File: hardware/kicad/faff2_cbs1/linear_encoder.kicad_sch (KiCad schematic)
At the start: 26 parts, among them J601 FH12-10S-0.5SH(55), J602 FTSH-105-01-L-DV-K-TR, U601 AM26LV32

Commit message: review r1: logic-analyser headers, U501 reference note, AFE/encoder fixes
Answers the captain's round-1 review points on loadcell_afe, linear_encoder,
temp_sense and nvm_calibration.

U501 and the reference (R1). The ADS1235 has no internal reference and no
reference output pin - REFP0/REFN0 are inputs. The reference is the load cell's
own excitation, sensed at the bridge, which is what makes the measurement
ratiometric. Documented in a 15-line note beside U501B's reference pins.

Logic-analyser headers (R2, R5). The Amodo keyed 10-way 0.1in socket
(8510-4500PL) replaces the per-net hooks:

  J502  loadcell_afe   CH0..CH7 = the whole SPI3 interface plus nDRDY, START,
                       nRESET and CLKIN; TP506..TP512 and TP514 removed
  J603  linear_encoder CH0..CH4 = the three receiver outputs plus ENC_SDO and
                       ENC_nPROG; TP602..TP607 removed

Both tap the driver side of the series terminators, so the header still sees the
bus when an isolation link is lifted. J602 is KEPT: it carries REQ-PS-09, its
pin 9 is +5V_ENC where the socket wants GND, and six of its signals are the
terminated RS-422 pairs that DEC-0018 ruling 1 keeps stub-free. Raised as a
decision; ruled option (a) and captain-ratified.

J601 (R3, R4). Reference text moved off the body; the project-local
FH12-10S-0.5SH(55) symbol now shows pin numbers and names every pin (1..10,
MP1/MP2), matching the FH35C house exemplar. Fixed in faff2_periph.kicad_sym
and in the sheet's embedded copy, so no lib_symbol_mismatch.

5 V read-head supply (R6). R608, R609 and D602 are DNP parallel positions on
R601, FB601 and D601. Not for current sharing - the ferrite alone has 4x margin
on the CALC budget - but for bring-up: a shunt at R608 meters head current in
circuit, R609 bypasses the bead, D602 is a second SC-79 clamp. Moving D601 up
to make room also cleared its value text off the ENC_nPROG label and its ground
triangle off the ENC_nPROG wire.

temp_sense C701/C702 (R7). Both had their groun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
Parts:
- removed TP602: TestPoint, Amodo:TestPoint_Pad_D1.0mm, symbol Amodo_Connectors:TestPoint
- removed TP603, TP604, TP605, TP606, TP607: TestPoint, Amodo:KeystoneMiniatureTestLoop, symbol Amodo_Connectors:TestPointHook
- added D602: PESD5V0U1UB, Amodo:SC-79 (SOD523), symbol Amodo_Diodes:PESD5V0U1UB
- added J603: 8510-4500PL, Amodo:8510-4500PL_LOGIC_TEST, symbol Amodo_Connectors:Header_Female_10-way_2-row_Straight_2.54mm_THT__KEYED_LOGIC_TE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
- added R608, R609: 0R, Amodo:R_0603_1608Metric, symbol Amodo_Resistors:RES_TF_0R_0603
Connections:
- net +5V: now also R608.1
- net +5V_ENC: now also D602.1 (K), R609.2
- net ENC_SDO: now also J603.4 (CH3)
- net ENC_nPROG: now also J603.5 (CH4)
- net GND: now also D602.2 (A), J603.10 (GND), J603.9 (GND)
- net LINEAR_ENCODER_A: now also J603.1 (CH0)
- net LINEAR_ENCODER_B: now also J603.2 (CH1)
- net LINEAR_ENCODER_Z: now also J603.3 (CH2)
- net at FB601.1, R601.2: now also R608.2, R609.1
- no-connect marks 1 -> 4
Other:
- note added: "J603 - LOGIC-ANALYSER HEADER Amodo keyed 0.1in socket, 8510-4500PL. One plug replaces the old TP602..TP607 hooks, so a logic analyser goes on in one go. CH0 LINEAR_ENCODER_A CH1 LINEAR_ENCODER_B CH2 LINEAR_ENCODER_Z CH3 ENC_SDO CH4 ENC_nPROG CH5..CH7 spare (no-connect) 9, 10 GND for the leads Only single-ended nets are tapped: a 2.54 mm stub on a terminated 1 MHz RS-422 pair is the discontinuity 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"
- note added: "R608 / R609 / D602 are DNP parallel positions on R601 / FB601 / D601. Fit a shunt at R608 and lift R601 to meter head current in circuit; fit R609 to bypass the bead; D602 is a second SC-79 clamp position. None fitted by default."
- note removed: "GND hooks for scope / logic-analyser clips."
- moved on the sheet: D601, TP601

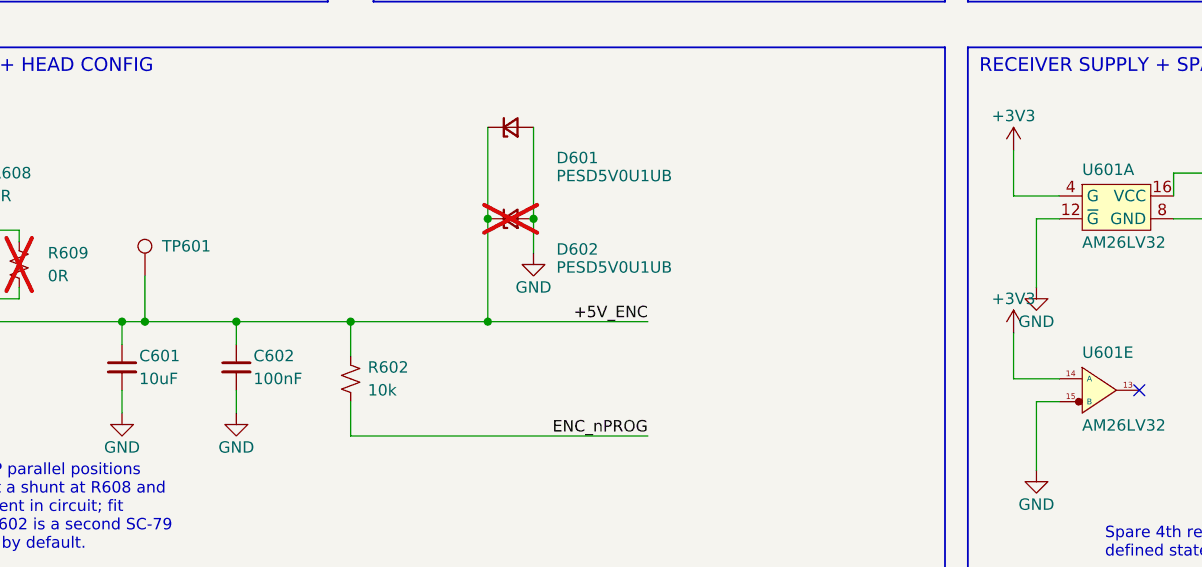
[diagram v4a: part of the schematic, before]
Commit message: review r1 final sweep: power labels, TP silkscreen names, text overlaps
The captain's design-wide pass, run once the per-sheet batches had landed.
Presentation only: ERC 0 errors / 0 warnings at severity-all, 404 components,
251 nets, and every per-net node set identical to the pre-sweep export.

  power labels   92 rail names were hidden on loadcell_afe, motor_drive and
                 temp_sense - all 285 power symbols now read, placed to the
                 house pattern (GND below the symbol, rail arrows above)
  test points    66 of 83 still carried the library default "TestPoint". All
                 83 now name what they measure, from the net they actually
                 land on in the netlist; longest is 5 characters
  text overlap   16 collisions cleared design-wide, four of them sub-millimetre
                 ones the bundled checker passes because it under-measures text
  GND upside down  none - 0 of 285 power symbols is rotated or mirrored
  graphic/wire   one: power_rails block D's bottom border lay along the last
                 PWR_FLAG's wire; the flag column moved up 2.54

The overlap checker turns out to have three separable blind spots, each settled
here by measuring a render rather than by reading the format: it grows every
text field rightward regardless of justify/mirror/180-rotation, so its box is a
mirror image of the truth for those and it both invents and misses collisions;
it measures text at ~1.06 mm per character where the real advance is ~1.19; and
it reflects a rotated symbol's body about the origin. tools/sch_geom.py models
all three correctly and the design is clean under it design-wide. Two of that
model's own rules - notes growing up from their anchor, and labels taking no
180-degree justify flip - were bugs of mine that the checker caught first. The
render is what settles it; neither tool is authoritative alone.

Placement is searched rather than guessed: 177 newly visible fields are tried
against every wire, block border, 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
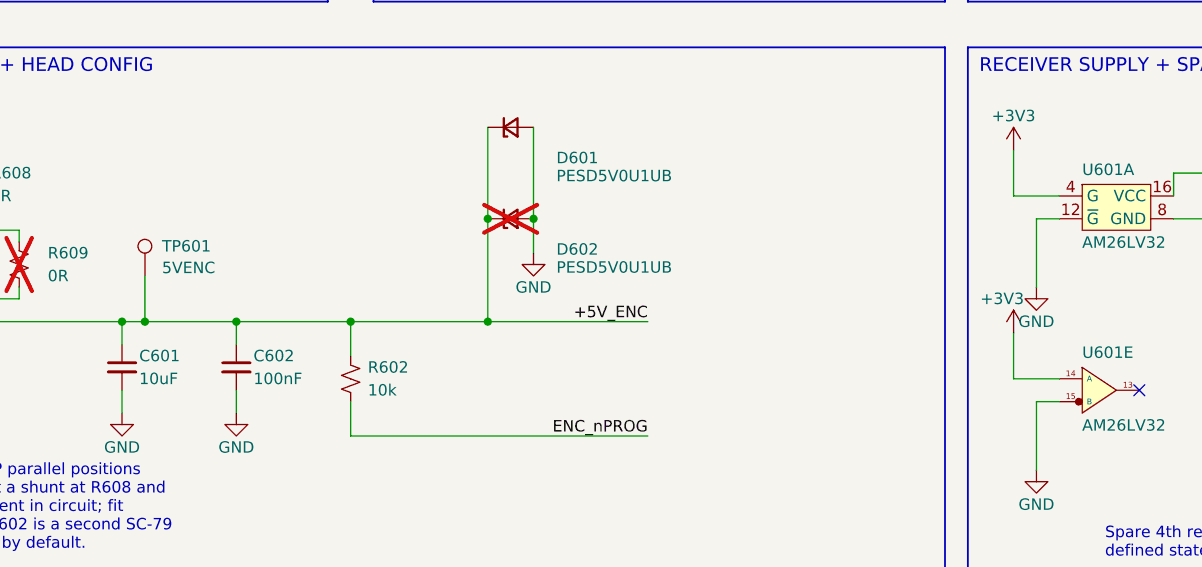
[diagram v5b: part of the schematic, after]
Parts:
- TP601: value TestPoint -> 5VENC
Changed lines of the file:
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@@
 			)
 		)
-		(property "Value" "TestPoint"
-			(at 58.4200 157.4800 0)
-			(effects
-				(font
-					(size 1.27 1.27)
-				)
-				(hide yes)
+		(property "Value" "5VENC"
+			(at 60.32 161.66 0)
+			(effects
+				(font
+					(size 1.27 1.27)
+				)
+				(justify left)
 			)
 		)
@@
 		)
 		(property "Value" "+3V3"
-			(at 154.9400 165.1000 0)
-			(effects
-				(font
+			(at 153.67 165.1 0)
+			(effects
+				(font

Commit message: review r2 items 4-7: four per-sheet placement fixes
  4  linear_encoder - U601A's GND body ended at y=166.37 and U601E's +3V3 body
     began at exactly 166.37, so the two flags were touching. The whole U601E
     group drops 7.62 - unit, both flags, four wires, and the no_connect on its
     unused output, which does NOT ride with the symbol: ERC caught that as
     pin_not_connected plus a dangling no-connect the first time round.
  5  temp_sense - C704/C705's grounds sat 0.6 mm above the REFP row with
     TP705's reference on the row itself; the caps and grounds move up 5.08.
     Three verticals ran through the block title, so it is shortened to
     "CHANNEL 2 FILTER + SHARED REF", which at size 1.778 ends at x=135.9 and
     clears the leftmost of them at 137.16.
  6  ui_io - R915's reference sat on its own body. It is the horizontal 0R
     variant but its fields were still on the vertical pattern; moved to the
     _H symbol's own pattern.
  7  motor_drive - #PWR1109/#PWR1110 bodies ended exactly on the block border
     and their GND text was outside the box entirely. Both move up to 138.43.

ERC 0 errors / 0 warnings at severity-all; 412 components, 259 nets, node sets
identical - all four are placement only.

Co-Authored-By: Claude Opus 5 <noreply@anthropic.com>
Claude-Session: https://claude.ai/code/session_01PFWfwT8RZc8Zqn8vgZxV8j
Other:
- moved on the sheet: U601E
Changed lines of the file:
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@@
 		)
 	)
-	(wire
-		(pts
-			(xy 160.0200 173.9900) (xy 154.9400 173.9900)
-		)
-		(stroke
-			(width 0)
-			(type default)
-		)
-	)
-	(wire
-		(pts
-			(xy 154.9400 173.9900) (xy 154.9400 168.9100)
-		)
-		(stroke
-			(width 0)
-			(type default)
-		)
-	)
-	(wire
-		(pts
-			(xy 160.0200 176.5300) (xy 157.4800 176.5300)
-		)
-		(stroke
-			(width 0)
-			(type default)
-		)
-	)
-	(wire
-		(pts
-			(xy 157.4800 176.5300) (xy 157.4800 184.1500)
-		)
-		(stroke
-			(width 0)
-			(type default)
-		)
-	)
 	(no_connect
-		(at 168.9100 175.2600)
+		(at 168.91 182.88)
 	)
 	(text "Spare 4th receiver: inputs held in a\ndefined state, output unused."
@@
 			)
 	)
+	(wire
+		(pts
+			(xy 154.94 176.53) (xy 154.94 181.61)
+		)
+		(stroke
+			(width 0)
+			(type default)
+		)
+	)
+	(wire
+		(pts
+			(xy 154.94 181.61) (xy 160.02 181.61)
+		)
+		(stroke
+			(width 0)
+			(type default)
+		)
+	)
+	(wire
+		(pts
+			(xy 157.48 184.15) (xy 157.48 191.77)
+		)
+		(stroke
+			(width 0)
+			(type default)
+		)
+	)
+	(wire
+		(pts
+			(xy 157.48 184.15) (xy 160.02 184.15)
+		)
+		(stroke
+			(width 0)
+			(type default)
+		)
+	)
 	(symbol
 		(lib_id "faff2_periph:FH12-10S-0.5SH(55)")
@@
 	(symbol
 		(lib_id "Amodo_Digital_ICs:AM26LS32Ax")
-		(at 162.5600 172.7200 0)
+		(at 162.56 180.34 0)
 		(unit 5)
 		(exclude_from_sim no)
@@
 		(dnp no)
 		(property "Reference" "U601"
-			(at 162.5600 171.8200 0)
+			(at 162.56 179.44 0)
 			(effects
 				(font
@@
 		)
 		(property "Value" "AM26LV32"
-			(at 162.5600 178.4200 0)
+			(at 162.56 186.04 0)
 			(effects
 				(font
@@
 		)
 		(property "Footprint" "Amodo:SOIC-16-N"
-			(at 162.5600 172.7200 0)
+			(at 162.56 180.34 0)
 			(effects
 				(font
@@
 		)
 		(property "Datasheet" "https://www.ti.com/lit/ds/symlink/am26lv32.pdf"
-			(at 162.5600 172.7200 0)
+			(at 162.56 180.34 0)
 			(effects
 				(font
@@
 		)
 		(property "Description" "RS-422 Interface IC Quad Diff Line"
-			(at 162.5600 172.7200 0)
+			(at 162.56 180.34 0)
 			(effects
 				(font
@@
 		)
 		(property "mpn" "AM26LV32CDR"
-			(at 162.5600 172.7200 0)
+			(at 162.56 180.34 0)
 			(effects
 				(font
@@
 		)
 		(property "SymLifecycle" "draft"
-			(at 162.5600 172.7200 0)
+			(at 162.56 180.34 0)
 			(effects
 				(font
@@
 	(symbol
 		(lib_id "Amodo_Symbols:+3V3")
-		(at 154.9400 168.9100 0)
+		(at 154.94 176.53 0)
 		(unit 1)
 		(exclude_from_sim no)
@@
 		(dnp no)
 		(property "Reference" "#PWR617"
-			(at 154.9400 162.5600 0)
+			(at 154.94 176.53 0)
 			(effects
 				(font
@@
 		)
 		(property "Value" "+3V3"
-			(at 153.67 165.1 0)
+			(at 154.94 172.72 0)
 			(effects
 				(font
@@
 		)
 		(property "Footprint" ""
-			(at 154.9400 168.9100 0)
+			(at 154.94 176.53 0)
 			(effects
 				(font
@@
 		)
 		(property "Datasheet" "~"
-			(at 154.9400 168.9100 0)
+			(at 154.94 176.53 0)
 			(effects
 				(font
@@
 		)
 		(property "Description" ""
-			(at 154.9400 168.9100 0)
+			(at 154.94 176.53 0)
 			(effects
 				(font
@@
 		)
 		(property "SymLifecycle" "tested"
-			(at 154.9400 168.9100 0)
+			(at 154.94 176.53 0)
 			(effects
 				(font
@@
 	(symbol
 		(lib_id "Amodo_Symbols:GND")
-		(at 157.4800 184.1500 0)
+		(at 157.48 191.77 0)
 		(unit 1)
 		(exclude_from_sim no)
@@
 		(dnp no)
 		(property "Reference" "#PWR618"
-			(at 157.4800 190.5000 0)
+			(at 157.48 191.77 0)
 			(effects
 				(font
@@
 		)
 		(property "Value" "GND"
-			(at 157.4800 187.9600 0)
+			(at 157.48 195.58 0)
 			(effects
 				(font
@@
 		)
 		(property "Footprint" ""
-			(at 157.4800 184.1500 0)
+			(at 157.48 191.77 0)
 			(effects
 				(font
@@
 		)
 		(property "Datasheet" "~"
-			(at 157.4800 184.1500 0)
+			(at 157.48 191.77 0)
 			(effects
 				(font
@@
 		)
 		(property "Description" "Power symbol creates a global label with name \"GND\" , ground"
-			(at 157.4800 184.1500 0)
+			(at 157.48 191.77 0)
 			(effects
 				(font
@@
 		)
 		(property "SymLifecycle" "tested"
-			(at 157.4800 184.1500 0)
+			(at 157.48 191.77 0)
 			(effects
 				(font
